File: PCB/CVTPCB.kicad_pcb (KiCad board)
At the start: 2 copper layers, 68 x 88 mm, 24 parts, among them J1 Infared, J2 TMP36, J3 Infared, J4 Conn_01x04_Pin, J5 TMP36, J7 SystemInput

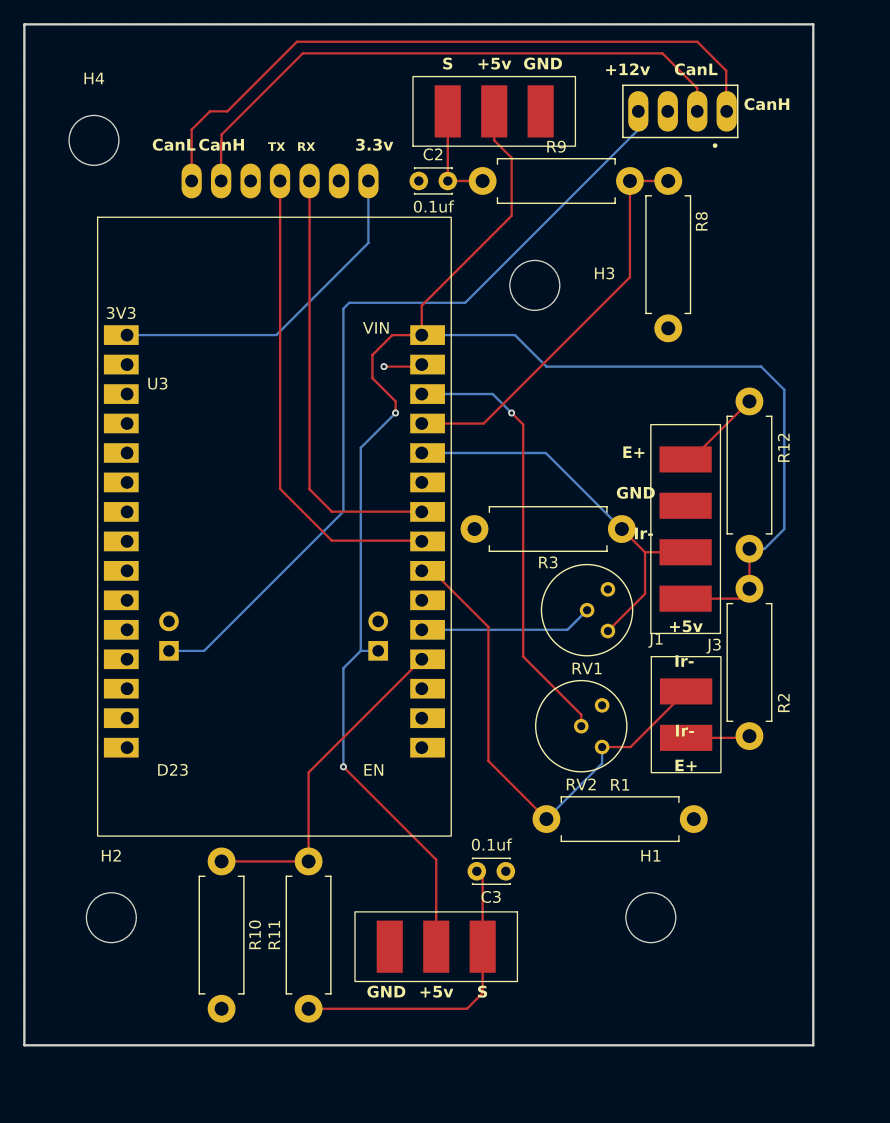
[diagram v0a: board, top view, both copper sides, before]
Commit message: Various changes to PCB design
Changes:
Move 4 pin aviation plug connector to bottom of PCB
Move 0.1uF bypass capacitors from Vout to Vs
Remove voltage divider on TMP36 output. TMP36 output ranges from 0.1V to 2.0V, which is within our 0-3.3V reading range on ESP32
Change signal voltage divider for IR receiver from 1W footprint to 1/4W footprint
Combine +5V and GND pads for IR and TMP36
Update Silkscreen and Labels for clarity
Make Power pads SMD
Move all components to top side
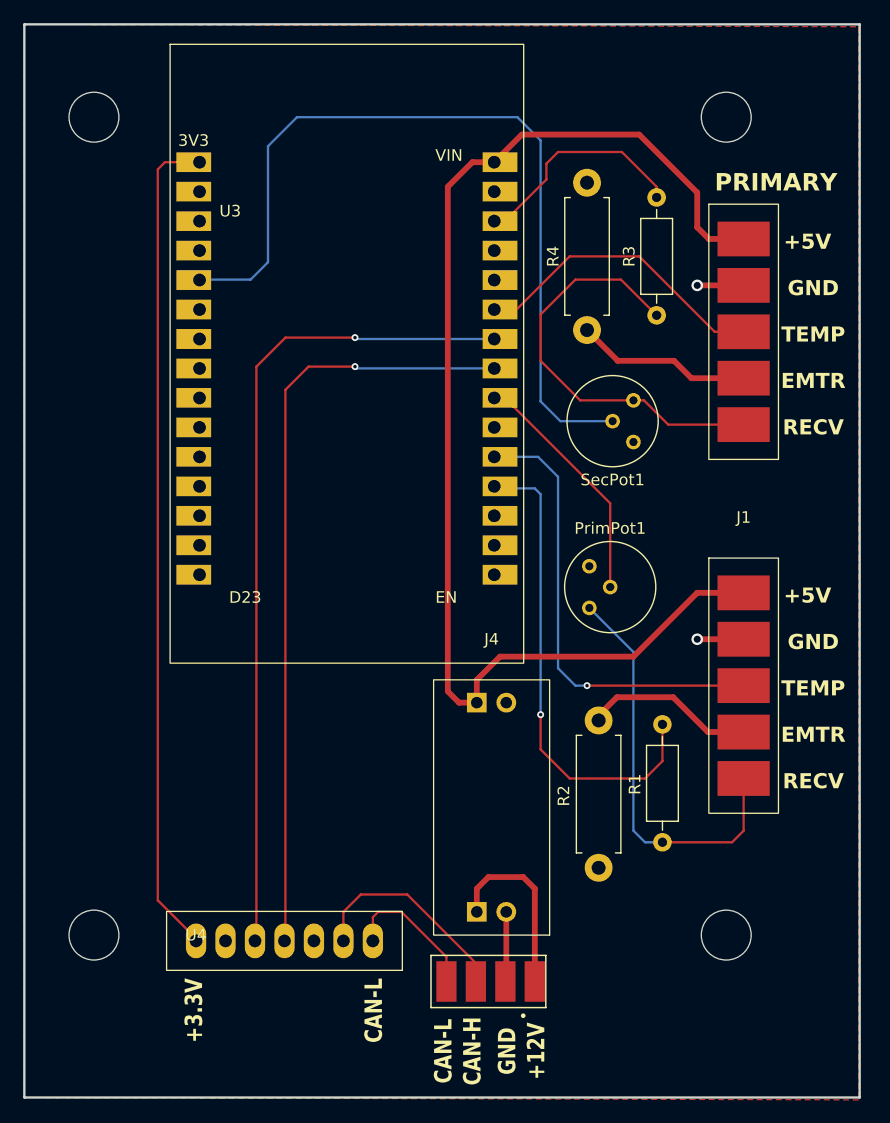
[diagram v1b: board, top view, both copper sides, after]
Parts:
- removed C2, C3: 0.1uf, Capacitor_THT:C_Disc_D3.0mm_W2.0mm_P2.50mm
- removed J2, J5: TMP36, CVT:TMP36_Pad
- removed R10, R8: 300, Resistor_THT:R_Axial_DIN0411_L9.9mm_D3.6mm_P12.70mm_Horizontal
- removed R11, R9: 200, Resistor_THT:R_Axial_DIN0411_L9.9mm_D3.6mm_P12.70mm_Horizontal
- removed R12: 22, Resistor_THT:R_Axial_DIN0411_L9.9mm_D3.6mm_P12.70mm_Horizontal
- removed RV2: 0-10k, Potentiometer_THT:Potentiometer_Bourns_3339H_Vertical
- added PrimPot1: 0-10k, Potentiometer_THT:Potentiometer_Bourns_3339H_Vertical, F.Cu at (148.7, 102.8)
- added R4: 22, Resistor_THT:R_Axial_DIN0411_L9.9mm_D3.6mm_P12.70mm_Horizontal, F.Cu at (148.5, 78.8)
- J1: value Infared -> PrimaryPads; footprint CVT:Infared -> CVT:Temp_IR_5_Pad_Combo
- J3: value Infared -> SecondaryPads; footprint CVT:Infared -> CVT:Temp_IR_5_Pad_Combo
- J4: value Conn_01x04_Pin -> 12V_5V_Regulator; moved to F.Cu
- R1, R3: footprint Resistor_THT:R_Axial_DIN0411_L9.9mm_D3.6mm_P12.70mm_Horizontal -> Resistor_THT:R_Axial_DIN0207_L6.3mm_D2.5mm_P10.16mm_Horizontal
- U4: moved to F.Cu
- moved J7 76.8 mm to (140.0, 135.0)
- moved U4 67.2 mm to (114.8, 131.5), turned to 0 degrees
- moved J3 43.3 mm to (162.0, 65.0), turned to 0 degrees
- moved H3 22.0 mm to (160.5, 60.5)
- moved R3 18.7 mm to (154.5, 77.6), turned to 90 degrees
- moved SecPot1 16.4 mm to (152.5, 84.9)
- moved U3 16.2 mm to (127.8, 64.4)
- moved R2 13.1 mm to (149.5, 112.5), turned to -90 degrees
- moved R1 10.2 mm to (155.0, 123.0), turned to 90 degrees
- moved J1 9.84 mm to (162.0, 95.5)
- moved H1 6.67 mm to (160.5, 131.0)
- moved J4 4.87 mm to (140.3, 106.0), turned to 0 degrees
- moved H2 2.12 mm to (106.0, 131.0)
- moved H4 2.00 mm to (106.0, 60.5)
- renumbered RV1 to SecPot1
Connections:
- net /CanRX renamed Net-(U3-D26)
- net /CanTX renamed Net-(U3-D25)
- J1 pad 2: /IrOut1 -> GND
- J3 pad 2: /IrOut2 -> GND
- J3 pad 3: GND -> Net-(J3-Pin_3)
- J4 pad 3: /+12v -> Net-(J4-Pin_3)
- J7 pad 1: /CanL -> Net-(J4-Pin_3)
- J7 pad 2: /CanH -> GND
- J7 pad 3: GND -> Net-(J7-Pin_3)
- J7 pad 4: /+12v -> Net-(J7-Pin_4)
- R1 pad 1: /IrOut1 -> Net-(J1-Pin_5)
- R1 pad 2: GND -> Net-(U3-D34)
- R2 pad 2: +5V -> GND
- R3 pad 1: /IrOut2 -> Net-(J3-Pin_5)
- R3 pad 2: GND -> Net-(U3-D13)
- SecPot1 pad 1: GND -> Net-(J3-Pin_5)
- SecPot1 pad 2: /Ir1 -> Net-(U3-D4)
- SecPot1 pad 3: /IrOut2 -> GND
- U3 pad 19: /TMP36_1 -> Net-(U3-D34)
- U3 pad 20: /Ir1 -> Net-(J1-Pin_3)
- U3 pad 22: /IrOut1 -> Net-(U3-D33)
- U3 pad 25: unconnected-(U3-D27-Pad25) -> Net-(J3-Pin_3)
- U3 pad 26: /IrOut2 -> unconnected-(U3-D14-Pad26)
- U3 pad 27: /TMP36_2 -> unconnected-(U3-D12-Pad27)
- U3 pad 28: /Ir2 -> Net-(U3-D13)
- U3 pad 5: unconnected-(U3-D4-Pad5) -> Net-(U3-D4)
- U4 pad 6: /CanH -> Net-(J7-Pin_3)
- U4 pad 7: /CanL -> Net-(J7-Pin_4)
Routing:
- net Net-(U3-D4): track 0.00 -> 71.3 mm
- net /+12v: track 70.9 -> 0.00 mm
- net /CanL: track 58.2 -> 0.00 mm
- net /CanH: track 51.2 -> 0.00 mm
- net /IrOut1: track 43.8 -> 0.00 mm
- net Net-(U3-D34): track 0.00 -> 41.6 mm, vias 0 -> 1
- net +3.3V: track 30.4 -> 71.7 mm
- net Net-(J1-Pin_3): track 0.00 -> 39.3 mm, vias 0 -> 1
- net /Ir2: track 37.9 -> 0.00 mm, vias 1 -> 0
- net +5V: track 144.8 -> 107.3 mm, vias 2 -> 0
- net Net-(J3-Pin_5): track 0.00 -> 36.3 mm
- net Net-(J1-Pin_5): track 0.00 -> 35.6 mm
- net /TMP36_2: track 34.8 -> 0.00 mm
- net /IrOut2: track 34.4 -> 0.00 mm
- net Net-(U3-D26): track 37.1 -> 71.4 mm, vias 0 -> 1
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- added copper zone on F.Cu, net (none)
- added copper zone on B.Cu, net GND
- removed copper zone on F.Cu, net GND
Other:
- board size 68 x 88 mm -> 72 x 92.5 mm
- board text added: "+12V"
- board text added: "+3.3V"
- board text added: "+5V"
- board text added: "CAN-H"
- board text added: "CAN-L"
- board text added: "EMTR"
- board text added: "PRIMARY"
- board text added: "RECV"
- board text added: "TEMP"
- board text removed: "+12v"
- board text removed: "+5v"
- board text removed: "3.3v"
- board text removed: "CanH"
- board text removed: "CanL"
- board text removed: "E+"
- board text removed: "Ir-"
- board text removed: "RX"
- board text removed: "S"
- board text removed: "TX"

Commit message: Fix missing silkscreen and flipped orientation of pot
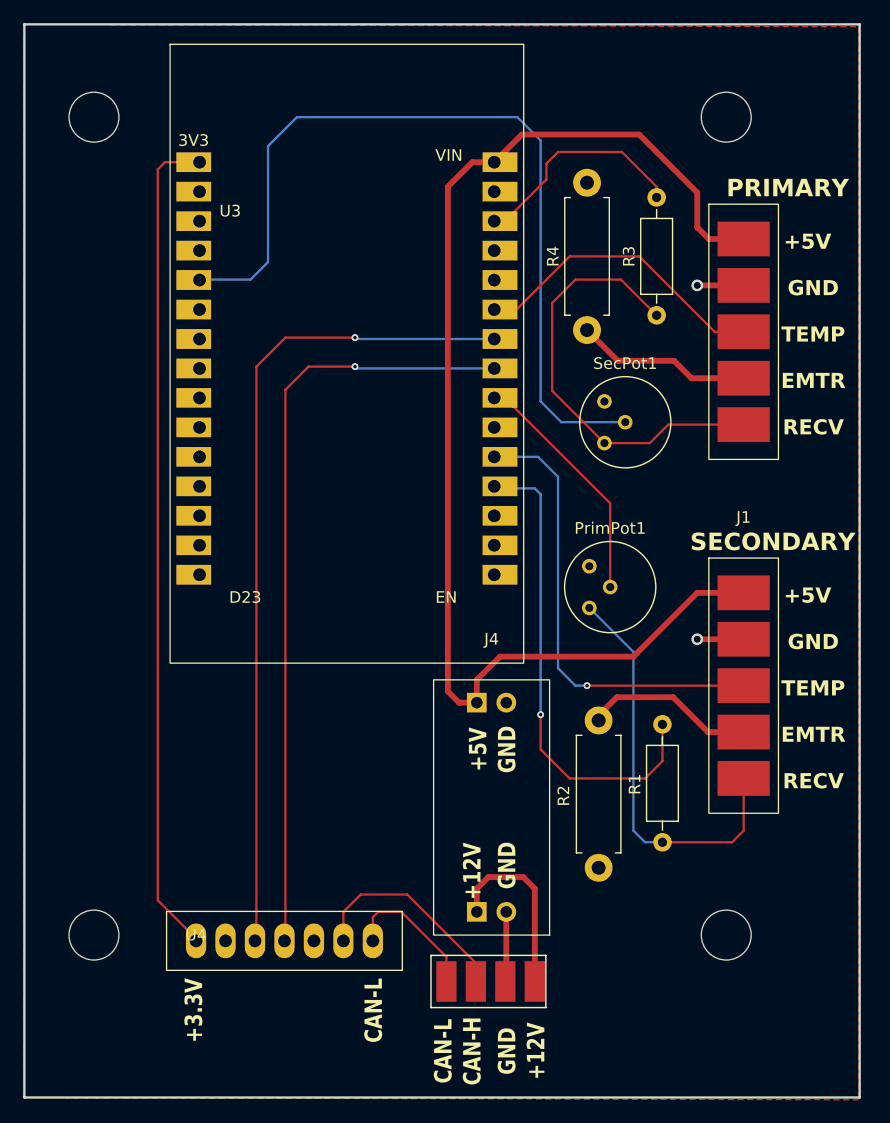
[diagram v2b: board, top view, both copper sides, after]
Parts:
- moved SecPot1 4.45 mm to (150.0, 88.6), turned to 0 degrees
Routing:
- net Net-(J3-Pin_5): track 36.3 -> 37.7 mm
- net Net-(U3-D4): track 71.3 -> 72.4 mm
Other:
- board text added: "SECONDARY"
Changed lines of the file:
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@@
 			(usegerberattributes yes)
 			(usegerberadvancedattributes yes)
-			(creategerberjobfile yes)
+			(creategerberjobfile no)
 			(dashed_line_dash_ratio 12.000000)
 			(dashed_line_gap_ratio 3.000000)
@@
 			(plotinvisibletext no)
 			(sketchpadsonfab no)
-			(subtractmaskfromsilk no)
+			(subtractmaskfromsilk yes)
 			(outputformat 1)
 			(mirror no)
-			(drillshape 1)
+			(drillshape 0)
 			(scaleselection 1)
 			(outputdirectory "")
@@
 			(layer "F.SilkS")
 		)
-		(fp_circle
-			(center 3 2.95)
-			(end 3.1 2.95)
-			(stroke
-				(width 0.2)
-				(type solid)
-			)
-			(fill none)
-			(layer "F.SilkS")
-		)
 		(fp_line
 			(start -5.2 -2.5)
@@
 			(layer "F.Fab")
 		)
-		(fp_circle
-			(center 3 2.95)
-			(end 3.1 2.95)
-			(stroke
-				(width 0.2)
-				(type solid)
-			)
-			(fill none)
-			(layer "F.Fab")
-		)
 		(pad "1" smd rect
 			(at 4 0 180)
@@
 	(footprint "Potentiometer_THT:Potentiometer_Bourns_3339H_Vertical"
 		(layer "F.Cu")
-		(at 152.5 84.907898 180)
+		(at 150 88.592102)
 		(descr "Potentiometer, vertical, Bourns 3339H, http://www.bourns.com/docs/Product-Datasheets/3339.pdf")
 		(tags "Potentiometer vertical Bourns 3339H")
 		(property "Reference" "SecPot1"
-			(at 1.796051 -6.856051 0)
+			(at 1.796051 -6.856051 360)
 			(layer "F.SilkS")
 			(effects
@@
 		)
 		(property "Value" "0-10k"
-			(at 1.796051 3.263949 0)
+			(at 1.796051 3.263949 360)
 			(layer "F.Fab")
 			(effects
@@
 		)
 		(property "Footprint" "Potentiometer_THT:Potentiometer_Bourns_3339H_Vertical"
-			(at 0 0 180)
+			(at 0 0 0)
 			(unlocked yes)
 			(layer "F.Fab")
@@
 		)
 		(property "Datasheet" ""
-			(at 0 0 180)
+			(at 0 0 0)
 			(unlocked yes)
 			(layer "F.Fab")
@@
 		)
 		(property "Description" "Potentiometer"
-			(at 0 0 180)
+			(at 0 0 0)
 			(unlocked yes)
 			(layer "F.Fab")
@@
 		)
 		(fp_line
-			(start 5.9 2.3)
-			(end 5.9 -5.9)
+			(start -2.3 -5.9)
+			(end -2.3 2.3)
 			(stroke
 				(width 0.05)
@@
 		)
 		(fp_line
-			(start 5.9 -5.9)
-			(end -2.3 -5.9)
+			(start -2.3 2.3)
+			(end 5.9 2.3)
 			(stroke
 				(width 0.05)
@@
 		)
 		(fp_line
-			(start -2.3 2.3)
-			(end 5.9 2.3)
+			(start 5.9 -5.9)
+			(end -2.3 -5.9)
 			(stroke
 				(width 0.05)
@@
 		)
 		(fp_line
-			(start -2.3 -5.9)
-			(end -2.3 2.3)
+			(start 5.9 2.3)
+			(end 5.9 -5.9)
 			(stroke
 				(width 0.05)
@@
 		)
 		(fp_circle
-			(center 1.797 -1.795102)
-			(end 4.297 -1.795102)
+			(center 1.796051 -1.796051)
+			(end 5.606051 -1.796051)
 			(stroke
 				(width 0.1)
@@
 		)
 		(fp_circle
-			(center 1.796051 -1.796051)
-			(end 5.606051 -1.796051)
+			(center 1.797 -1.795102)
+			(end 4.297 -1.795102)
 			(stroke
 				(width 0.1)
@@
 		)
 		(pad "1" thru_hole circle
-			(at 0 0 180)
+			(at 0 0)
 			(size 1.26 1.26)
 			(drill 0.7)
@@
 		)
 		(pad "2" thru_hole circle
-			(at 1.796051 -1.796051 180)
+			(at 1.796051 -1.796051)
 			(size 1.26 1.26)
 			(drill 0.7)
@@
 		)
 		(pad "3" thru_hole circle
-			(at 0 -3.592102 180)
+			(at 0 -3.592102)
 			(size 1.26 1.26)
 			(drill 0.7)
@@
 	)
 	(gr_text "PRIMARY"
-		(at 159.5 67 0)
+		(at 160.5 67.5 0)
 		(layer "F.SilkS")
 		(effects
@@
 		)
 	)
+	(gr_text "+12V"
+		(at 139.5 125.5 90)
+		(layer "F.SilkS")
+		(effects
+			(font
+				(size 1.5 1.2)
+				(thickness 0.3)
+				(bold yes)
+			)
+			(justify bottom)
+		)
+	)
 	(gr_text "+5V"
 		(at 167.5 72 0)
@@
 		)
 	)
+	(gr_text "GND"
+		(at 142.5 115 90)
+		(layer "F.SilkS")
+		(effects
+			(font
+				(size 1.5 1.2)
+				(thickness 0.3)
+				(bold yes)
+			)
+			(justify bottom)
+		)
+	)
 	(gr_text "EMTR\n"
 		(at 168 114.5 0)
@@
 		)
 	)
+	(gr_text "SECONDARY"
+		(at 164.5 98 0)
+		(layer "F.SilkS")
+		(effects
+			(font
+				(size 1.5 1.5)
+				(thickness 0.3)
+				(bold yes)
+			)
+			(justify bottom)
+		)
+	)
 	(gr_text "GND"
 		(at 168 106.5 0)
@@
 	)
 	(gr_text "GND"
+		(at 142.5 125 90)
+		(layer "F.SilkS")
+		(effects
+			(font
+				(size 1.5 1.2)
+				(thickness 0.3)
+				(bold yes)
+			)
+			(justify bottom)
+		)
+	)
+	(gr_text "GND"
 		(at 142.5 141 90)
 		(layer "F.SilkS")
@@
 		)
 	)
+	(gr_text "+5V"
+		(at 140 115 90)
+		(layer "F.SilkS")
+		(effects
+			(font
+				(size 1.5 1.2)
+				(thickness 0.3)
+				(bold yes)
+			)
+			(justify bottom)
+		)
+	)
 	(gr_text "RECV\n"
 		(at 168 118.5 0)
@@
 	)
 	(segment
-		(start 144.5 62.5)
-		(end 142.5 60.5)
+		(start 121 73)
+		(end 119.5 74.5)
 		(width 0.2)
 		(layer "B.Cu")
@@
 	)
 	(segment
-		(start 123.5 60.5)
-		(end 121 63)
+		(start 151.796051 86.796051)
+		(end 146.296051 86.796051)
 		(width 0.2)
 		(layer "B.Cu")
@@
 	)
 	(segment
-		(start 115.14 74.5)
-		(end 115.1 74.54)
+		(start 146.296051 86.796051)
+		(end 144.5 85)
 		(width 0.2)
 		(layer "B.Cu")
@@
 	)
 	(segment
-		(start 146.203949 86.703949)
-		(end 144.5 85)
+		(start 144.5 62.5)
+		(end 142.5 60.5)
 		(width 0.2)
 		(layer "B.Cu")
@@
 	)
 	(segment
-		(start 142.5 60.5)
-		(end 123.5 60.5)
+		(start 115.14 74.5)
+		(end 115.1 74.54)
 		(width 0.2)
 		(layer "B.Cu")
@@
 	)
 	(segment
-		(start 150.703949 86.703949)
-		(end 146.203949 86.703949)
+		(start 119.5 74.5)
+		(end 115.14 74.5)
 		(width 0.2)
 		(layer "B.Cu")
@@
 	)
 	(segment
-		(start 121 73)
-		(end 119.5 74.5)
+		(start 142.5 60.5)
+		(end 123.5 60.5)
 		(width 0.2)
 		(layer "B.Cu")
@@
 	)
 	(segment
-		(start 119.5 74.5)
-		(end 115.14 74.5)
+		(start 123.5 60.5)
+		(end 121 63)
 		(width 0.2)
 		(layer "B.Cu")
@@
 	)
 	(segment
-		(start 144.5 77.5)
-		(end 144.5 81.5)
-		(width 0.2)
-		(layer "F.Cu")
-		(net 27)
-	)
-	(segment
-		(start 144.5 81.5)
-		(end 147.907898 84.907898)
+		(start 145.5 84.092102)
+		(end 150 88.592102)
 		(width 0.2)
 		(layer "F.Cu")
@@
 	)
 	(segment
-		(start 155.5 87)
-		(end 162 87)
+		(start 153.907898 88.592102)
+		(end 150 88.592102)
 		(width 0.2)
 		(layer "F.Cu")
@@
 	)
 	(segment
-		(start 147.907898 84.907898)
-		(end 152.5 84.907898)
+		(start 151.42 74.5)
+		(end 147.5 74.5)
 		(width 0.2)
 		(layer "F.Cu")
@@
 	)
 	(segment
-		(start 151.42 74.5)
-		(end 147.5 74.5)
+		(start 155.5 87)
+		(end 153.907898 88.592102)
 		(width 0.2)
 		(layer "F.Cu")
@@
 	)
 	(segment
-		(start 152.5 84.907898)
-		(end 153.407898 84.907898)
+		(start 155.5 87)
+		(end 162 87)
 		(width 0.2)
 		(layer "F.Cu")
@@
 	)
 	(segment
-		(start 147.5 74.5)
-		(end 144.5 77.5)
+		(start 145.5 76.5)
+		(end 145.5 84.092102)
 		(width 0.2)
 		(layer "F.Cu")
@@
 	)
 	(segment
-		(start 153.407898 84.907898)
-		(end 155.5 87)
+		(start 147.5 74.5)
+		(end 145.5 76.5)
 		(width 0.2)
 		(layer "F.Cu")
